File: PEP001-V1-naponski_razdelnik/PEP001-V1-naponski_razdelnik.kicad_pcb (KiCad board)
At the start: 2 copper layers, 45 x 45 mm, 12 parts, among them J1 Screw_Terminal_01x02

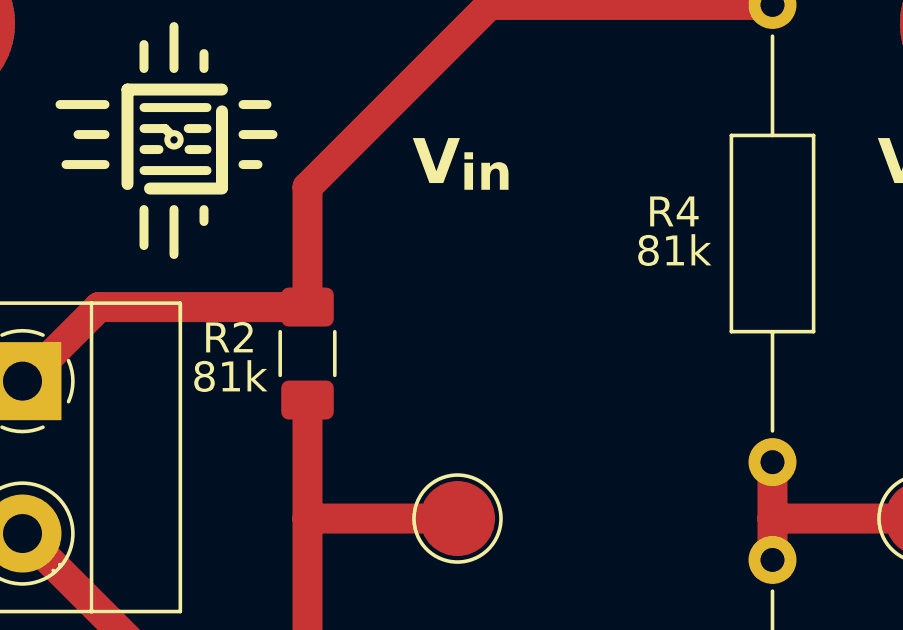
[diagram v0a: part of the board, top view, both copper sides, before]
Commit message: PEP001-V1_BOM_CPL
-Added JLC component numbers
-Generated BOM csv file for SMD components
-Generated CPL csv file for SMD components
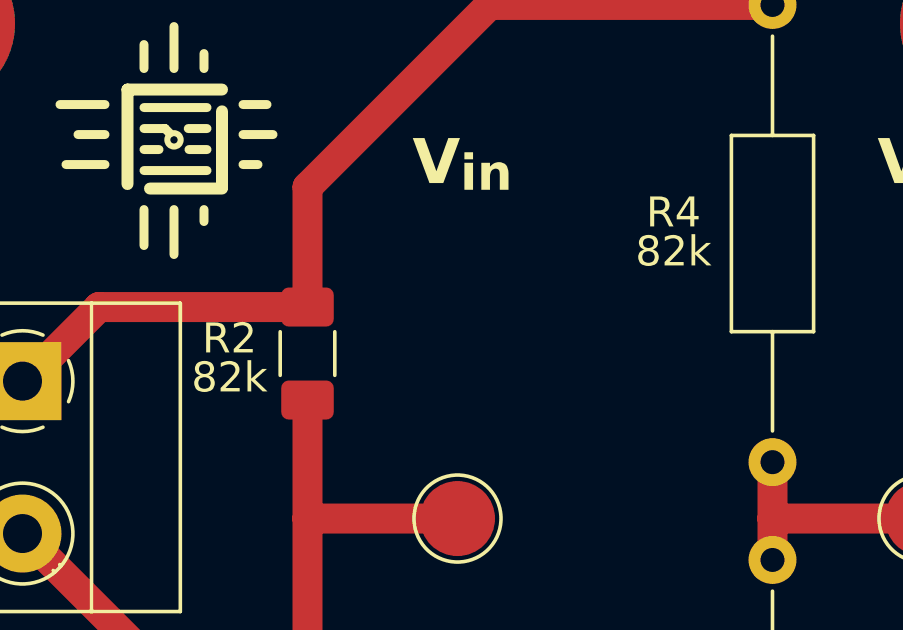
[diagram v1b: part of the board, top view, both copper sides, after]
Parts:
- R2, R4: value 81k -> 82k
